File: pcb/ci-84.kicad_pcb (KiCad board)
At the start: 2 copper layers, 91 x 217 mm, 118 parts, among them J1 jst-battery, J2 SWD, SW1 SW_Push, SW10 XT0N, SW11 STAT, SW12 MATH, SW13 APPS, SW14 PRGM, SW15 VARS, SW16 CLEAR, SW17 X^-1, SW18 SIN, SW19 COS, SW2 Y=, SW20 TAN, SW21 ^, SW22 X^2, SW23 ,, SW24 (, SW25 ), SW26 DIVIDE, SW27 LOG, SW28 7, SW29 8, SW3 WINDOW, SW30 9, SW31 MULITPLY, SW32 IN, SW33 4, SW34 5, SW35 6, SW36 SUBTRACT, SW37 STO, SW38 1, SW39 2, SW4 ZOOM, SW40 3, SW41 ADD, SW42 ON, SW43 0, SW44 ., SW45 (-), SW46 ENTER, SW47 GRAPH, SW48 UP, SW49 RIGHT, SW5 TRACE, SW50 DOWN, SW51 LEFT, SW6 2ND, SW7 MODE, SW8 DEL, SW9 ALPHA, U1 STM32L471RGTx, U3 TPS63900, U4 TFT_320x240

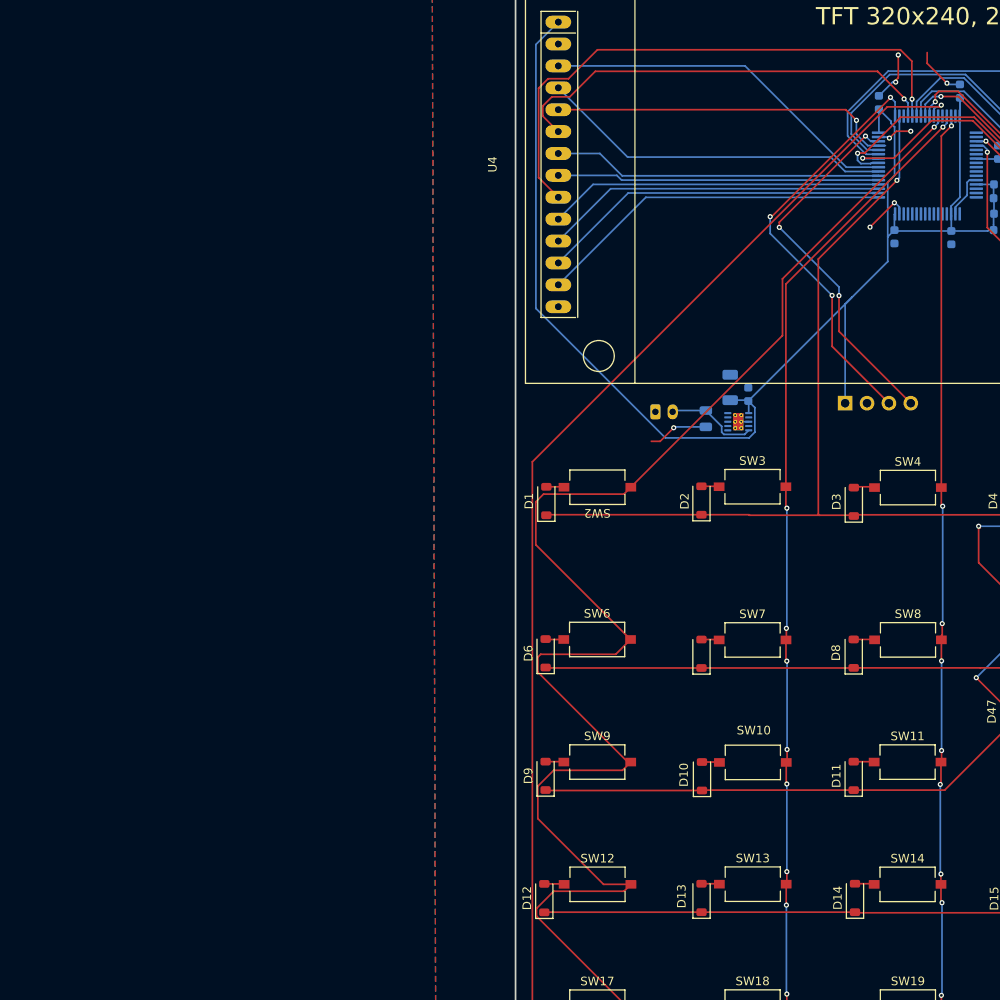
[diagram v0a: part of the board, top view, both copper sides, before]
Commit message: cleaned schematic and added final components
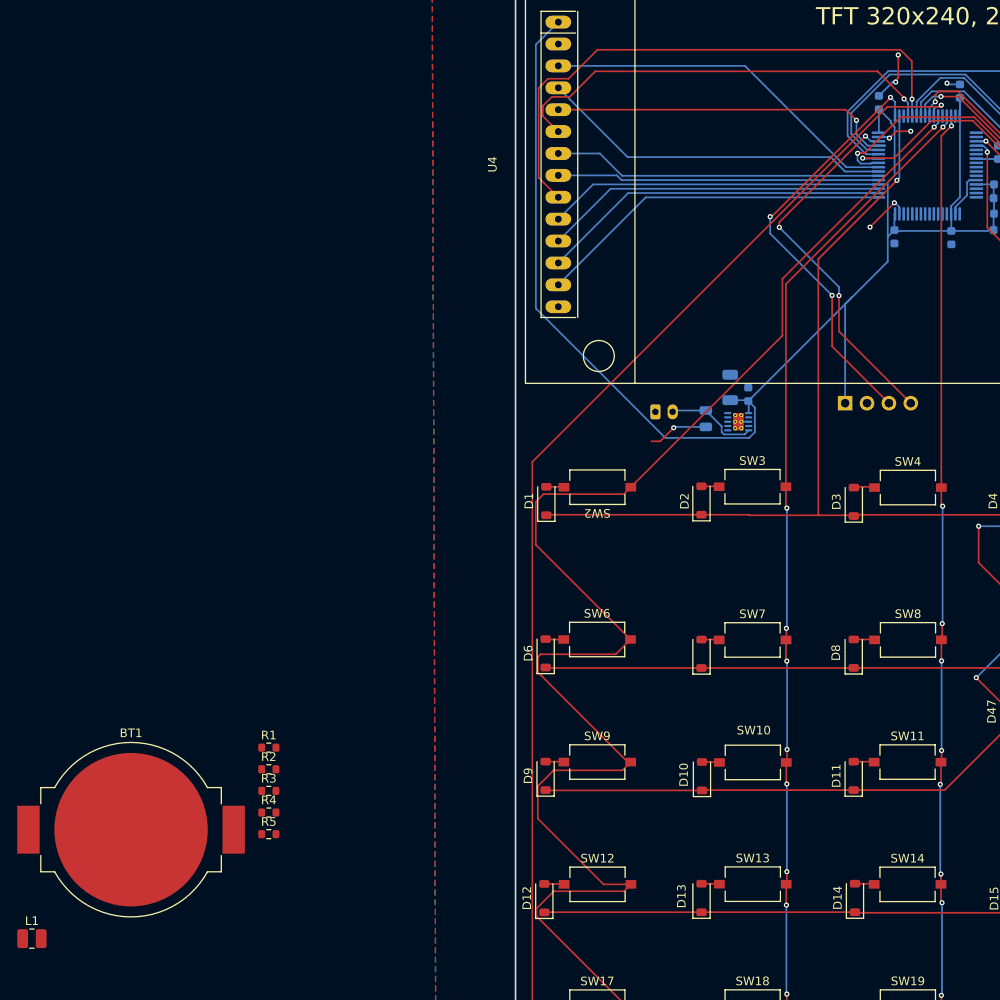
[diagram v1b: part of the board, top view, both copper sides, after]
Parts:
- added BT1: Battery_Cell, Battery:BatteryHolder_MPD_BC2003_1x2032, F.Cu at (192.9, 196.4)
- added L1: 2.2u, Inductor_SMD:L_1008_2520Metric, F.Cu at (181.4, 209.0)
- added R1: R, Resistor_SMD:R_0603_1608Metric, F.Cu at (208.9, 186.9)
- added R2: R, Resistor_SMD:R_0603_1608Metric, F.Cu at (208.9, 189.4)
- added R3: 1k, Resistor_SMD:R_0603_1608Metric, F.Cu at (208.9, 191.9)
- added R4: 2k, Resistor_SMD:R_0603_1608Metric, F.Cu at (208.9, 194.4)
- added R5: 36.5k, Resistor_SMD:R_0603_1608Metric, F.Cu at (208.9, 196.9)
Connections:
- U1 pad 1: unconnected-(U1-VBAT-Pad1) -> /VBAT
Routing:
- net GND: track 37.0 -> 32.5 mm

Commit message: finish all connections
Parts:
- L1, R1, R2, R3, R4, R5: moved to B.Cu
- moved BT1 117.5 mm to (295.8, 139.6)
- moved R4 108.3 mm to (288.9, 121.4), turned to -90 degrees
- moved R3 107.6 mm to (288.1, 119.1)
- moved R2 104.4 mm to (283.7, 116.5), turned to 180 degrees
- moved L1 104.2 mm to (266.6, 149.1), turned to -90 degrees
- moved R1 102.0 mm to (284.6, 118.5)
- moved R5 70.6 mm to (260.5, 148.7), turned to 90 degrees
- moved J1 2.40 mm to (251.3, 147.8)
- moved C11 2.13 mm to (257.4, 148.6)
- moved C12 0.62 mm to (262.0, 144.6)
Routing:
- net /VBAT: track 0.00 -> 61.7 mm, vias 0 -> 5
- net GND: track 32.5 -> 64.9 mm, vias 8 -> 10
- net VDD: track 170.0 -> 185.5 mm
- net Net-(U1-BOOT0): track 0.00 -> 8.29 mm
- net Net-(U1-PC0): track 0.00 -> 3.92 mm
- net Net-(U3-LX1): track 0.00 -> 2.34 mm
- net Net-(U3-LX2): track 0.00 -> 2.28 mm
- net +BATT: track 10.6 -> 12.6 mm
- net Net-(U3-CFG1): track 0.00 -> 1.80 mm
- net /c3: track 185.9 -> 186.5 mm
